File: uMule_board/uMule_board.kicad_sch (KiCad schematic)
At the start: 1 part, among them J1 12V IN

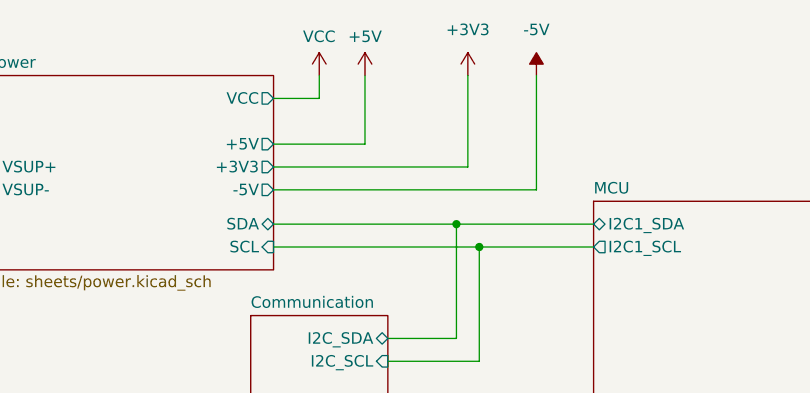
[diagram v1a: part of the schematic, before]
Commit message: another day, more progress. Elements are placed on board, traces need to be conected, added jumpers for power in case of bad design
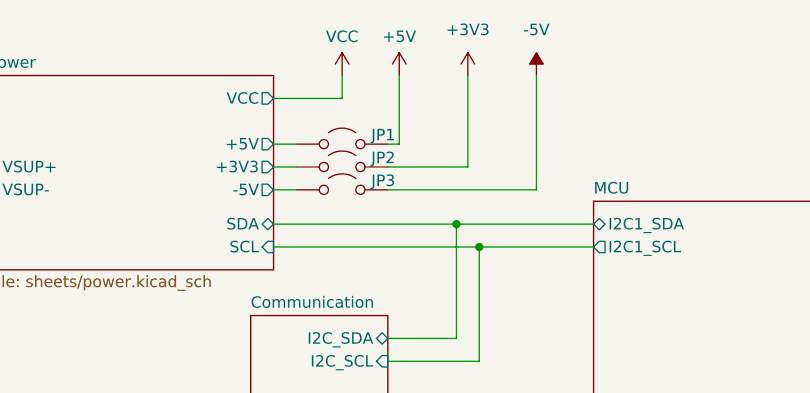
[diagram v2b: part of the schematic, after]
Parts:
- added JP1, JP2, JP3: Jumper_2_Open, TestPoint:TestPoint_2Pads_Pitch2.54mm_Drill0.8mm, symbol Jumper:Jumper_2_Open
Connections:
- net +3V3: now also JP2.2 (B)
- net +5V: now also JP1.2 (B)
- net -5V: now also JP3.2 (B)
- new net Power/+3V3: JP2.1 (A)
- new net Power/+5V: JP1.1 (A)
- new net Power/-5V: JP3.1 (A)

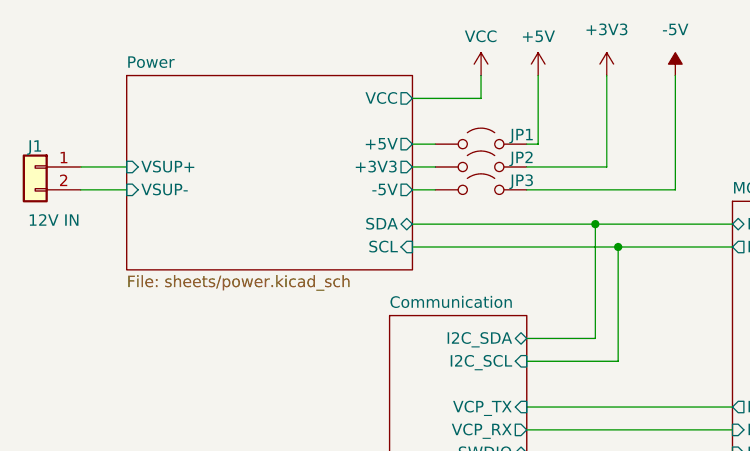
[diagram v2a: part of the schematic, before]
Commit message: DRC Passed, now only slight modifications on traces left, lenght matching and proper board description
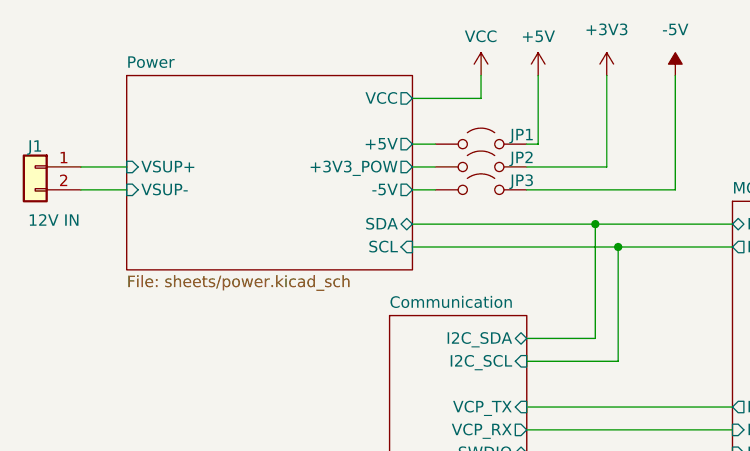
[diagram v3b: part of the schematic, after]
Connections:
- net Power/+3V3 renamed Power/+3V3_POW
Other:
- sheet Power ports: added +3V3_POW; removed +3V3
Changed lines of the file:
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@@
-			)
-		)
-		(pin "+3V3" output
-			(at 80.01 45.72 0)
-			(effects
-				(font
-					(size 1.27 1.27)
-				)
-				(justify right)
 			)
 		)
@@
 			(effects
 				(font
+					(size 1.27 1.27)
+				)
+				(justify right)
+			)
+		)
+		(pin "+3V3_POW" output
+			(at 80.01 45.72 0)
+			(effects
+				(font

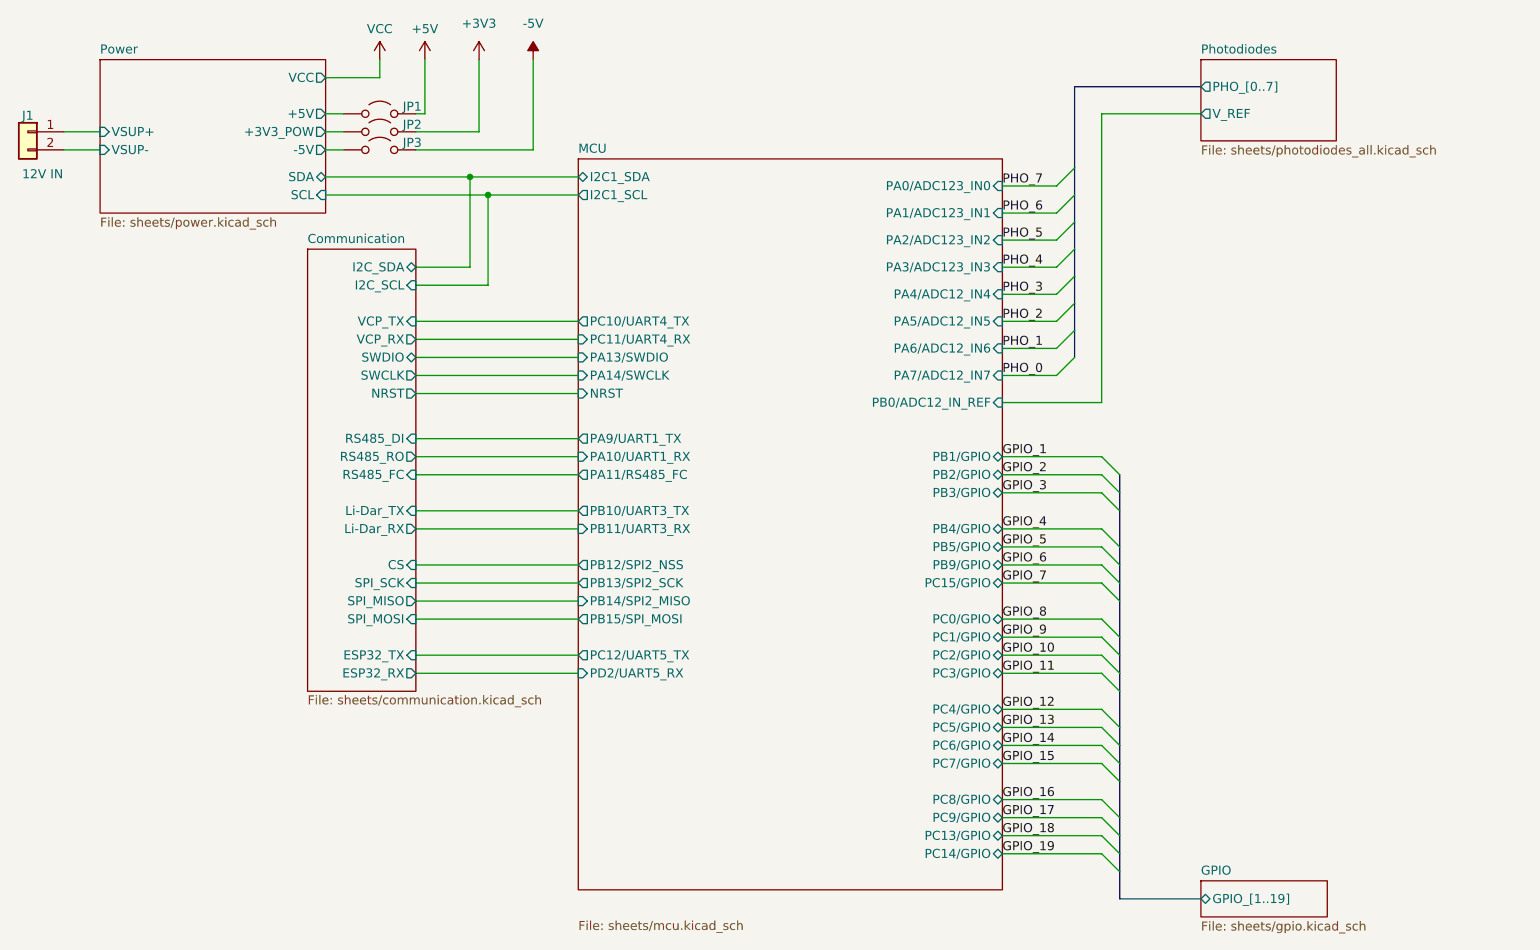
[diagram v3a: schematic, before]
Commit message: initial board is ready for conecting
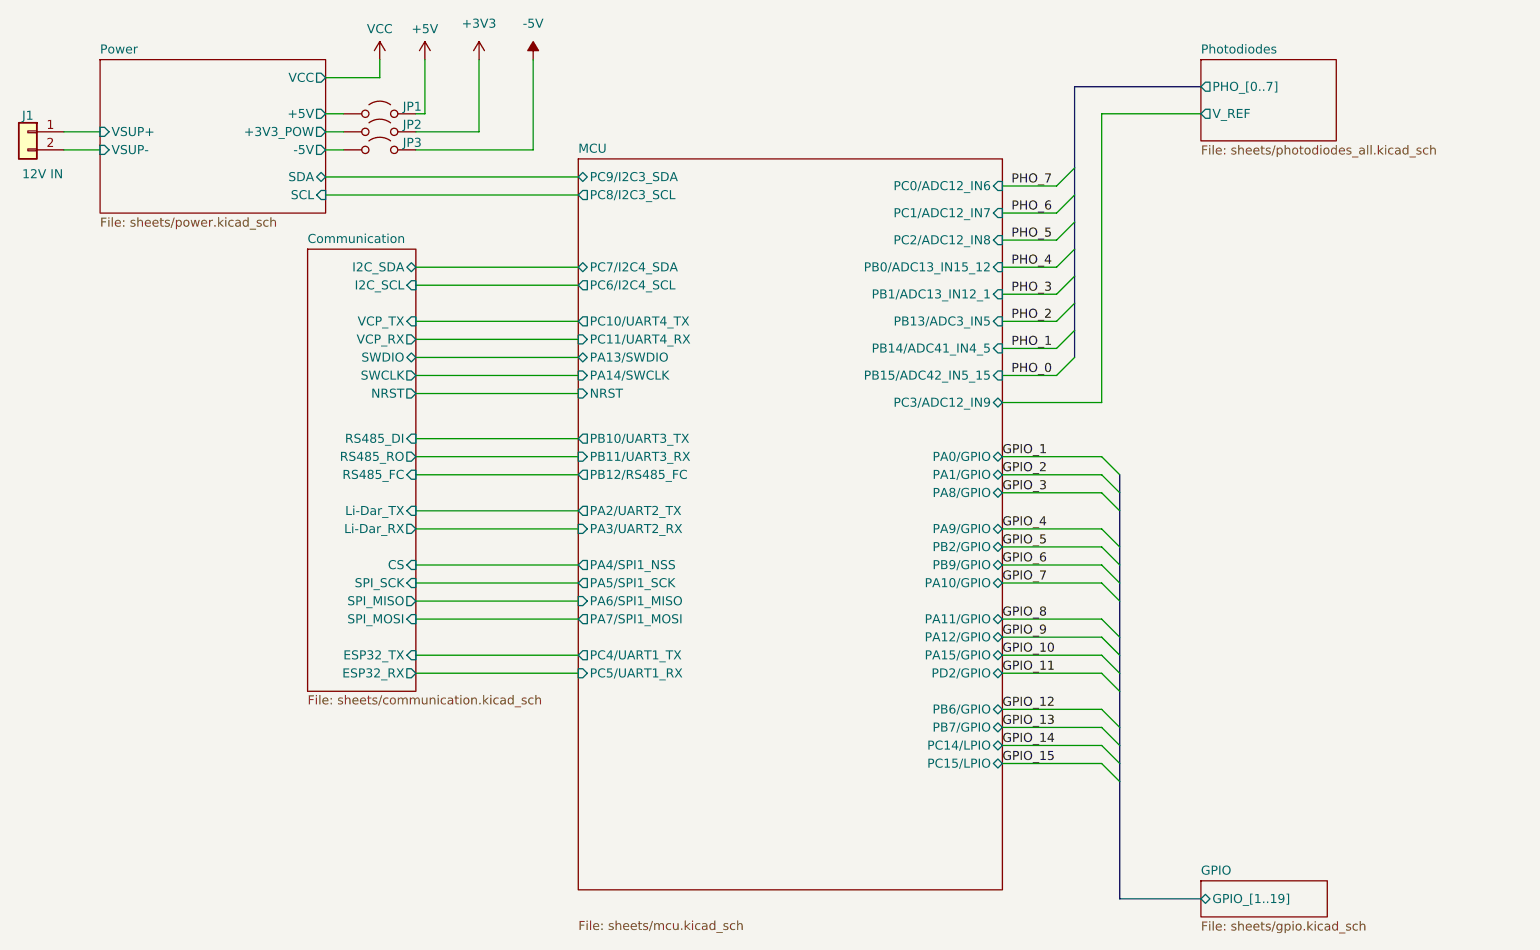
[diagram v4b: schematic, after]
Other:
- sheet MCU ports: added PA0/GPIO, PA10/GPIO, PA11/GPIO, PA12/GPIO, PA15/GPIO, PA1/GPIO, PA2/UART2_TX, PA3/UART2_RX, PA4/SPI1_NSS, PA5/SPI1_SCK, PA6/SPI1_MISO, PA7/SPI1_MOSI, PA8/GPIO, PA9/GPIO, PB0/ADC13_IN15_12, PB12/RS485_FC, PB13/ADC3_IN5, PB14/ADC41_IN4_5, PB15/ADC42_IN5_15, PB1/ADC13_IN12_1, PB6/GPIO, PB7/GPIO, PC0/ADC12_IN6, PC14/LPIO, PC15/LPIO, PC1/ADC12_IN7, PC2/ADC12_IN8, PC3/ADC12_IN9, PC4/UART1_TX, PC5/UART1_RX, PC6/I2C4_SCL, PC7/I2C4_SDA, PC8/I2C3_SCL, PC9/I2C3_SDA, PD2/GPIO; removed I2C1_SCL, I2C1_SDA, PA0/ADC123_IN0, PA10/UART1_RX, PA11/RS485_FC, PA1/ADC123_IN1, PA2/ADC123_IN2, PA3/ADC123_IN3, PA4/ADC12_IN4, PA5/ADC12_IN5, PA6/ADC12_IN6, PA7/ADC12_IN7, PA9/UART1_TX, PB0/ADC12_IN_REF, PB12/SPI2_NSS, PB13/SPI2_SCK, PB14/SPI2_MISO, PB15/SPI_MOSI, PB1/GPIO, PB3/GPIO, PB4/GPIO, PB5/GPIO, PC0/GPIO, PC12/UART5_TX, PC13/GPIO, PC14/GPIO, PC15/GPIO, PC1/GPIO, PC2/GPIO, PC3/GPIO, PC4/GPIO, PC5/GPIO, PC6/GPIO, PC7/GPIO, PC8/GPIO, PC9/GPIO, PD2/UART5_RX

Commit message: All elements connected. Now making more vias and corrections
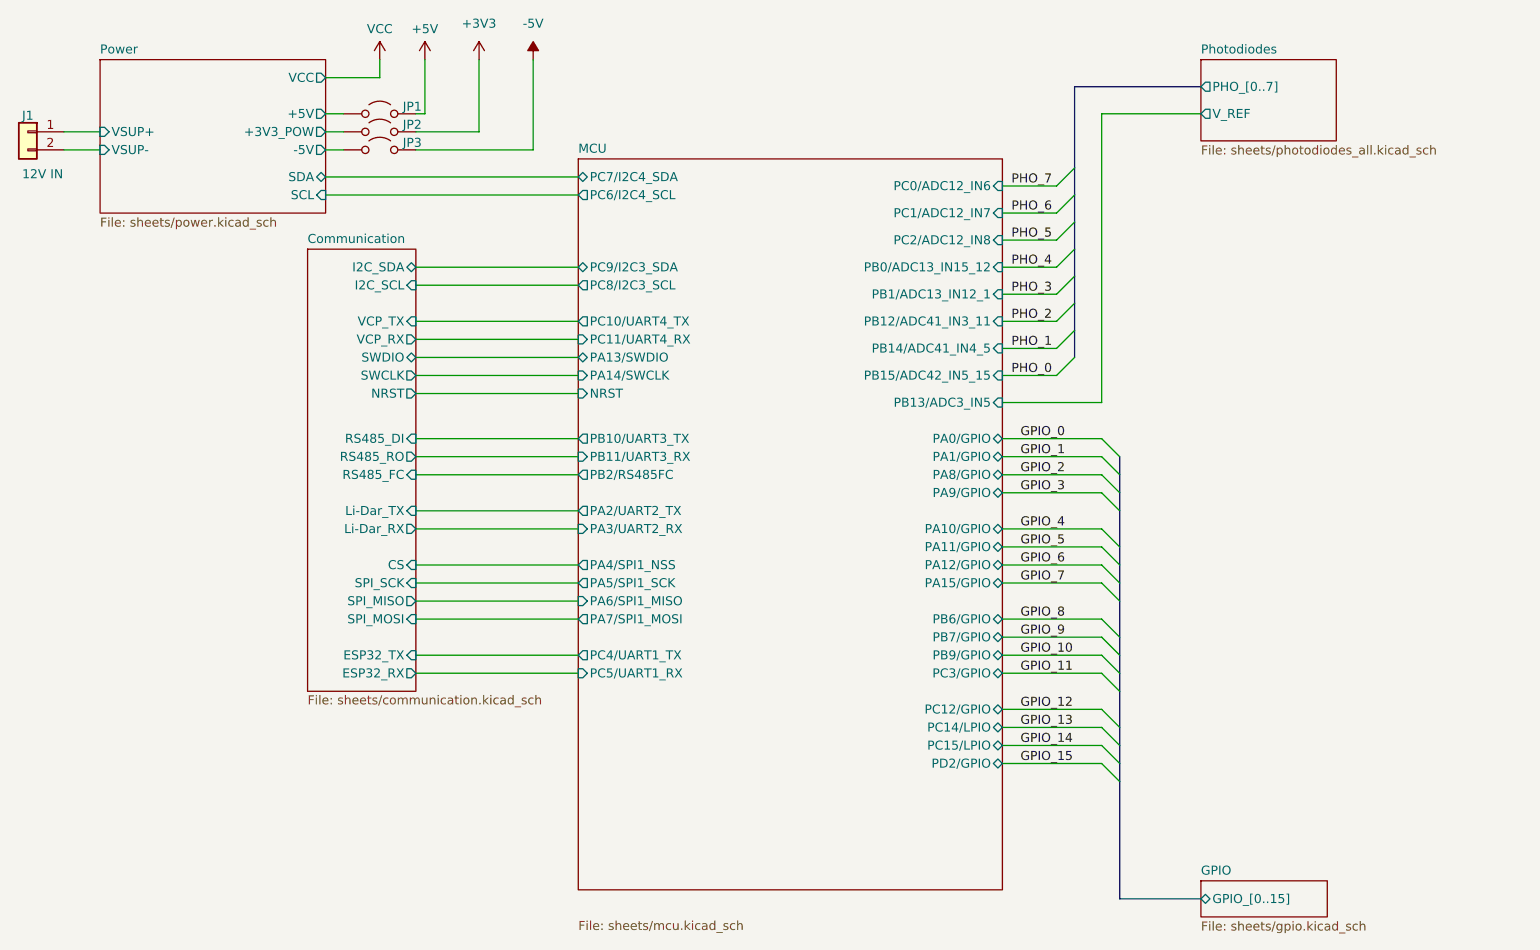
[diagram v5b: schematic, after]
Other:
- sheet GPIO ports: added GPIO_[0..15]; removed GPIO_[1..19]
- sheet MCU ports: added PB12/ADC41_IN3_11, PB2/RS485FC, PC12/GPIO, PC3/GPIO; removed PB12/RS485_FC, PB2/GPIO, PC3/ADC12_IN9
